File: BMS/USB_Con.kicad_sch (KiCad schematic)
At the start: 8 parts, among them J13 USB_A, J14 USB_C_Receptacle_USB2.0_14P

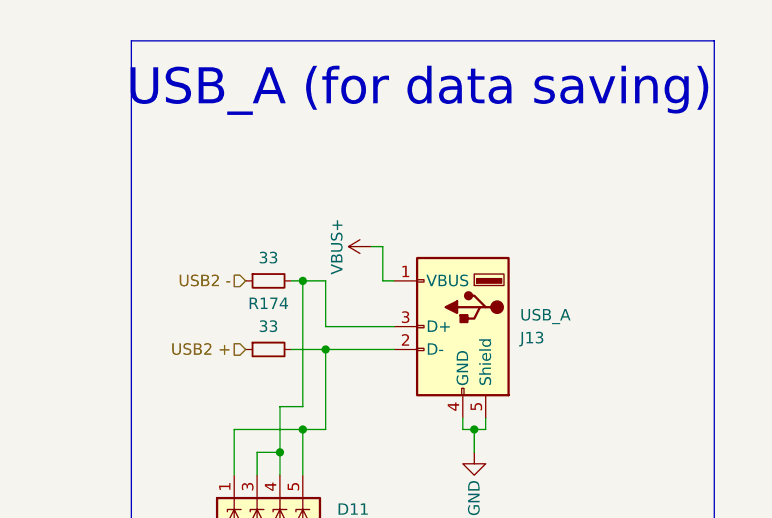
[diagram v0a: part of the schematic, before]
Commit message: Dodano layout drugiego bq79614, ukladu tlumaczącego z protokułu TI na UART oraz wstępnie poprowadzono pary różnicowe
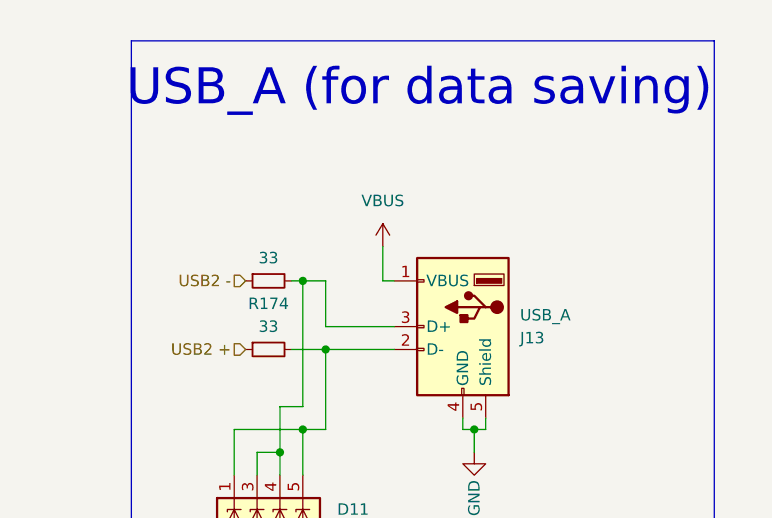
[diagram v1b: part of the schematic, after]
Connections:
- net VBUS: now reaches J13.1 (VBUS)
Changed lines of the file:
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@@
-	(wire
-		(pts
-			(xy 66.04 58.42) (xy 64.77 58.42)
-		)
-		(stroke
-			(width 0)
-			(type default)
-		)
-	)
 	(wire
 		(pts
@@
 	)
 	(symbol
+		(lib_id "power:VBUS")
+		(at 66.04 58.42 0)
+		(unit 1)
+		(exclude_from_sim no)
+		(in_bom yes)
+		(on_board yes)
+		(dnp no)
+		(fields_autoplaced yes)
+		(property "Reference" "#PWR035"
+			(at 66.04 62.23 0)
+			(effects
+				(font
+					(size 1.27 1.27)
+				)
+				(hide yes)
+			)
+		)
+		(property "Value" "VBUS"
+			(at 66.04 53.34 0)
+			(effects
+				(font
+					(size 1.27 1.27)
+				)
+			)
+		)
+		(property "Footprint" ""
+			(at 66.04 58.42 0)
+			(effects
+				(font
+					(size 1.27 1.27)
+				)
+				(hide yes)
+			)
+		)
+		(property "Datasheet" ""
+			(at 66.04 58.42 0)
+			(effects
+				(font
+					(size 1.27 1.27)
+				)
+				(hide yes)
+			)
+		)
+		(property "Description" "Power symbol creates a global label with name \"VBUS\""
+			(at 66.04 58.42 0)
+			(effects
+				(font
+					(size 1.27 1.27)
+				)
+				(hide yes)
+			)
+		)
+		(pin "1"
+		)
+		(instances
+			(project "BMS"
+				(path "/26289bb6-56bc-4ca1-b1a2-18d58d1afdf5/d34f5976-9b74-4159-94dc-792c476298a2/2f24219c-edc8-4bb8-8a5e-25aa99c199ab"
+					(reference "#PWR035")
+					(unit 1)
+				)
+			)
+		)
+	)
+	(symbol
 		(lib_id "Device:R_Small")
 		(at 144.78 72.39 90)
@@
 					(unit 1)
 				)
-			)
-		)
-	)
-	(symbol
-		(lib_id "power:+3.3V")
-		(at 64.77 58.42 90)
-		(unit 1)
-		(exclude_from_sim no)
-		(in_bom yes)
-		(on_board yes)
-		(dnp no)
-		(property "Reference" "#PWR0133"
-			(at 66.294 67.056 0)
-			(effects
-				(font
-					(size 1.27 1.27)
-				)
-				(hide yes)
-			)
-		)
-		(property "Value" "VBUS+"
-			(at 60.96 58.42 0)
-			(effects
-				(font
-					(size 1.27 1.27)
-				)
-			)
-		)
-		(property "Footprint" ""
-			(at 64.77 58.42 0)
-			(effects
-				(font
-					(size 1.27 1.27)
-				)
-				(hide yes)
-			)
-		)
-		(property "Datasheet" ""
-			(at 64.77 58.42 0)
-			(effects
-				(font
-					(size 1.27 1.27)
-				)
-				(hide yes)
-			)
-		)
-		(property "Description" ""
-			(at 64.77 58.42 0)
-			(effects
-				(font
-					(size 1.27 1.27)
-				)
-				(hide yes)
-			)
-		)
-		(pin "1"
-		)
-		(instances
-			(project "BMS"
-				(path "/26289bb6-56bc-4ca1-b1a2-18d58d1afdf5/d34f5976-9b74-4159-94dc-792c476298a2/2f24219c-edc8-4bb8-8a5e-25aa99c199ab"
-					(reference "#PWR0133")
-					(unit 1)
-				)

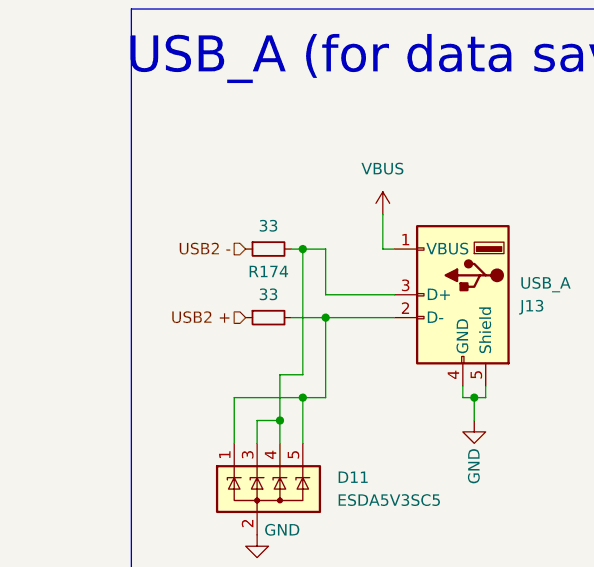
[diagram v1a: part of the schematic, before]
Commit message: Iteracja 1.0 gotowa, teraz sprawdzenie i zmiany kosmetyczne
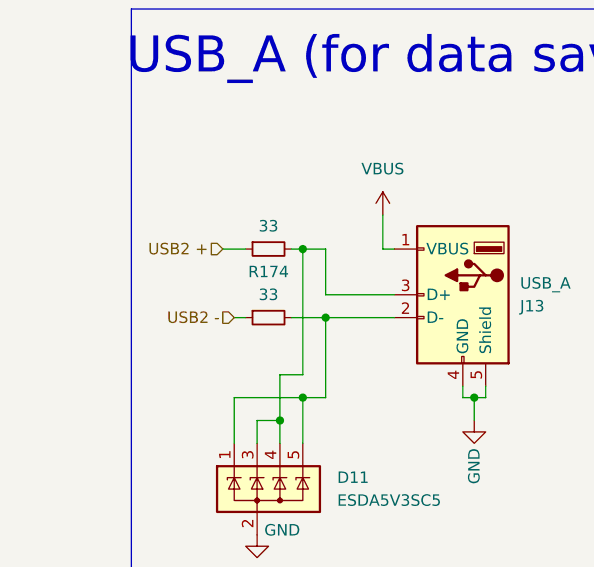
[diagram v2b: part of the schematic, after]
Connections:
- net USB2 +: now also R173.1; no longer R174.1
- net USB2 -: now also R174.1; no longer R173.1
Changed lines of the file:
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@@
+	(wire
+		(pts
+			(xy 48.26 62.23) (xy 50.8 62.23)
+		)
+		(stroke
+			(width 0)
+			(type default)
+		)
+	)
 	(wire
 		(pts
@@
 		(pts
 			(xy 74.93 77.47) (xy 74.93 78.74)
+		)
+		(stroke
+			(width 0)
+			(type default)
+		)
+	)
+	(wire
+		(pts
+			(xy 49.53 69.85) (xy 50.8 69.85)
 		)
 		(stroke
@@
 	(hierarchical_label "USB2 +"
 		(shape input)
-		(at 50.8 69.85 180)
+		(at 48.26 62.23 180)
 		(fields_autoplaced yes)
 		(effects
@@
 	(hierarchical_label "USB2 -"
 		(shape input)
-		(at 50.8 62.23 180)
+		(at 49.53 69.85 180)
 		(fields_autoplaced yes)
 		(effects
